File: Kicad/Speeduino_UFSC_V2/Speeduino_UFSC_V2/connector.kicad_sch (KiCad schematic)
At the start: 2 parts, among them J1 Conn_02x20_Counter_Clockwise, J2 Conn_01x02

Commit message: Add pdf
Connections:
- net FAN-OUT: now also J1.29 (Pin_29)
- net FUELPUMP-OUT: now also J1.31 (Pin_31)
- net TACHO-OUT: now also J1.33 (Pin_33)
- no-connect marks 0 -> 8

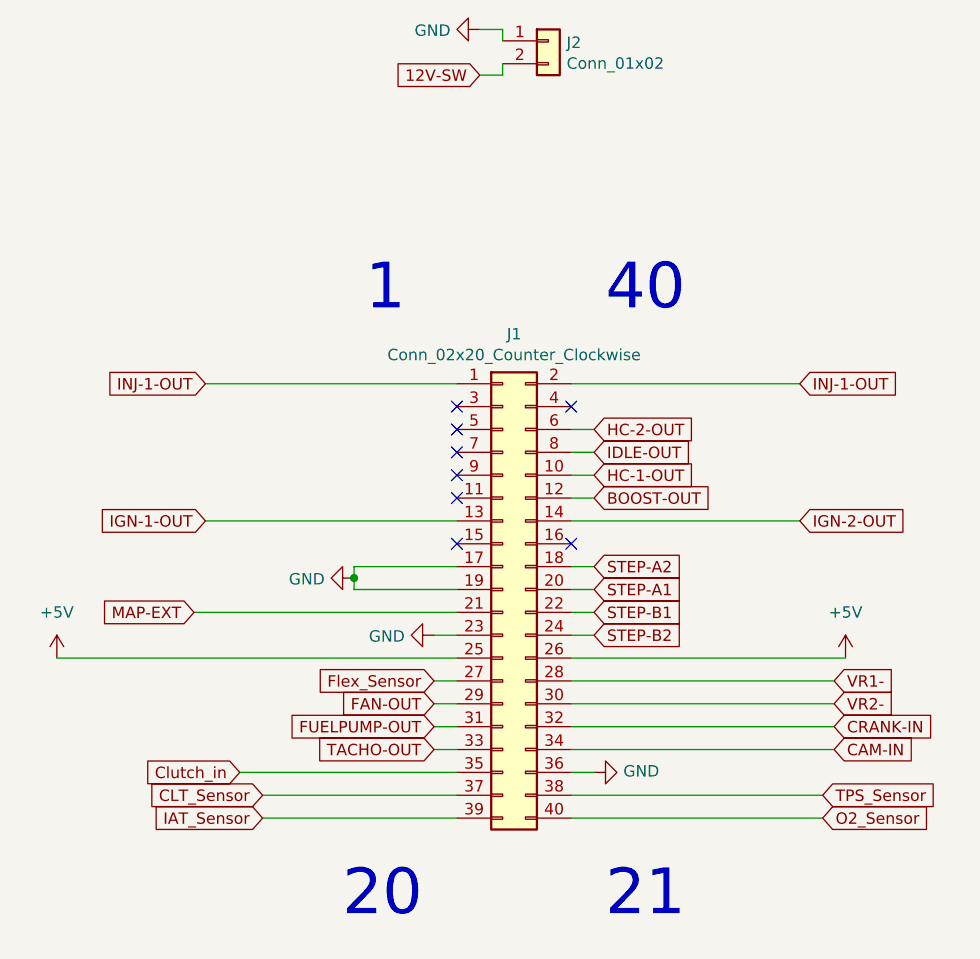
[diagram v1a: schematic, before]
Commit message: Add 2 injectors in schematic
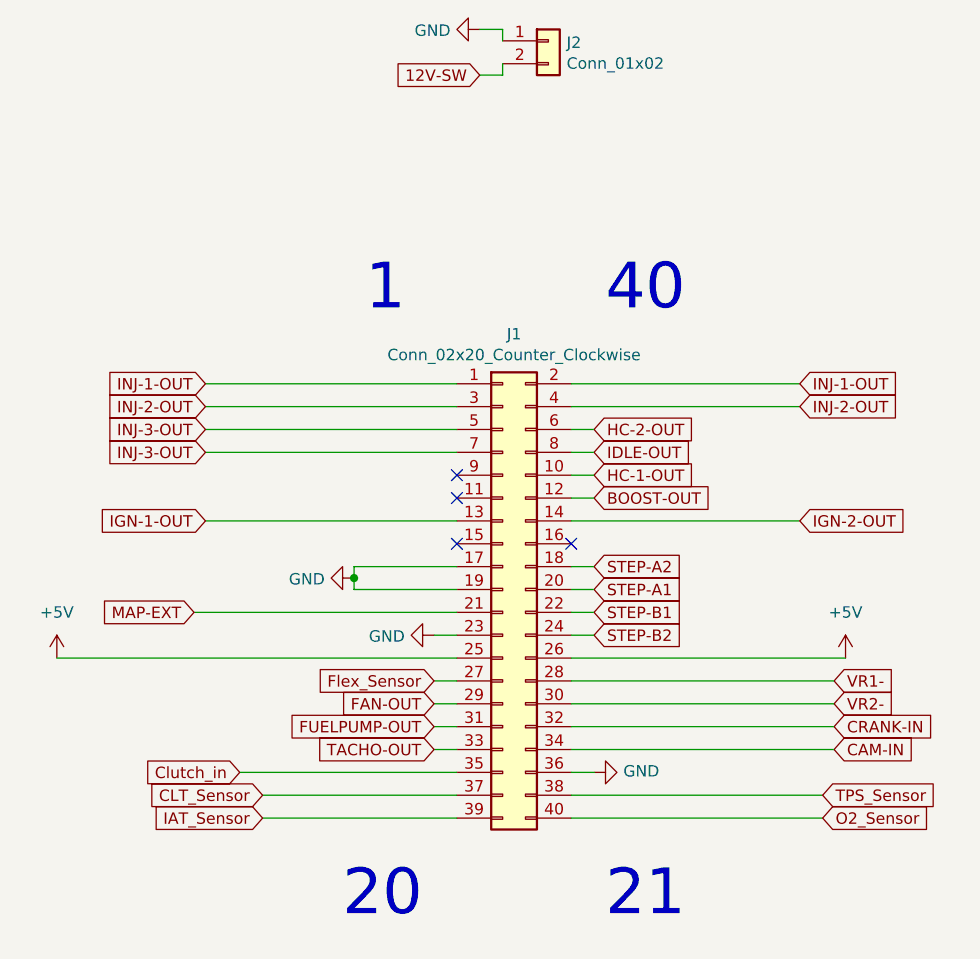
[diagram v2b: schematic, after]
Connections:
- net INJ-2-OUT: now reaches J1.3 (Pin_3)
- net INJ-2-OUT: now also J1.4 (Pin_4)
- net INJ-3-OUT: now reaches J1.5 (Pin_5)
- net INJ-3-OUT: now also J1.7 (Pin_7)
- no-connect marks 8 -> 4
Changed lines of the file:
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@@
-	)
-	(no_connect
-		(at 125.73 74.93)
 	)
 	(no_connect
@@
 	)
 	(no_connect
-		(at 125.73 77.47)
-	)
-	(no_connect
-		(at 138.43 74.93)
-	)
-	(no_connect
 		(at 125.73 85.09)
 	)
@@
 		(at 125.73 90.17)
 	)
-	(no_connect
-		(at 125.73 80.01)
-	)
 	(wire
 		(pts
@@
 	(wire
 		(pts
+			(xy 97.79 77.47) (xy 125.73 77.47)
+		)
+		(stroke
+			(width 0)
+			(type default)
+		)
+	)
+	(wire
+		(pts
 			(xy 97.79 72.39) (xy 125.73 72.39)
 		)
@@
 	(wire
 		(pts
+			(xy 97.79 74.93) (xy 125.73 74.93)
+		)
+		(stroke
+			(width 0)
+			(type default)
+		)
+	)
+	(wire
+		(pts
 			(xy 140.97 97.79) (xy 138.43 97.79)
 		)
@@
 	(wire
 		(pts
+			(xy 138.43 74.93) (xy 163.83 74.93)
+		)
+		(stroke
+			(width 0)
+			(type default)
+		)
+	)
+	(wire
+		(pts
 			(xy 123.19 100.33) (xy 125.73 100.33)
 		)
@@
 		(pts
 			(xy 138.43 95.25) (xy 140.97 95.25)
+		)
+		(stroke
+			(width 0)
+			(type default)
+		)
+	)
+	(wire
+		(pts
+			(xy 97.79 80.01) (xy 125.73 80.01)
 		)
 		(stroke
@@
 		)
 	)
+	(global_label "INJ-2-OUT"
+		(shape input)
+		(at 163.83 74.93 0)
+		(effects
+			(font
+				(size 1.27 1.27)
+			)
+			(justify left)
+		)
+		(property "Intersheetrefs" "${INTERSHEET_REFS}"
+			(at 163.83 74.93 0)
+			(effects
+				(font
+					(size 1.27 1.27)
+				)
+				(hide yes)
+			)
+		)
+	)
 	(global_label "HC-1-OUT"
 		(shape input)
@@
 			(effects
 				(font
+					(size 1.27 1.27)
+				)
+				(hide yes)
+			)
+		)
+	)
+	(global_label "INJ-3-OUT"
+		(shape input)
+		(at 97.79 77.47 180)
+		(effects
+			(font
+				(size 1.27 1.27)
+			)
+			(justify right)
+		)
+		(property "Intersheetrefs" "${INTERSHEET_REFS}"
+			(at 97.79 77.47 0)
+			(effects
+				(font
+					(size 1.27 1.27)
+				)
+				(hide yes)
+			)
+		)
+	)
+	(global_label "INJ-2-OUT"
+		(shape input)
+		(at 97.79 74.93 180)
+		(effects
+			(font
+				(size 1.27 1.27)
+			)
+			(justify right)
+		)
+		(property "Intersheetrefs" "${INTERSHEET_REFS}"
+			(at 97.79 74.93 0)
+			(effects
+				(font
+					(size 1.27 1.27)
+				)
+				(hide yes)
+			)
+		)
+	)
+	(global_label "INJ-3-OUT"
+		(shape input)
+		(at 97.79 80.01 180)
+		(effects
+			(font
+				(size 1.27 1.27)
+			)
+			(justify right)
+		)
+		(property "Intersheetrefs" "${INTERSHEET_REFS}"
+			(at 97.79 80.01 0)
+			(effects
+				(font
